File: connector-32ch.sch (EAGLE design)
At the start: 67 parts, among them X1 OMNETICS_36PAD

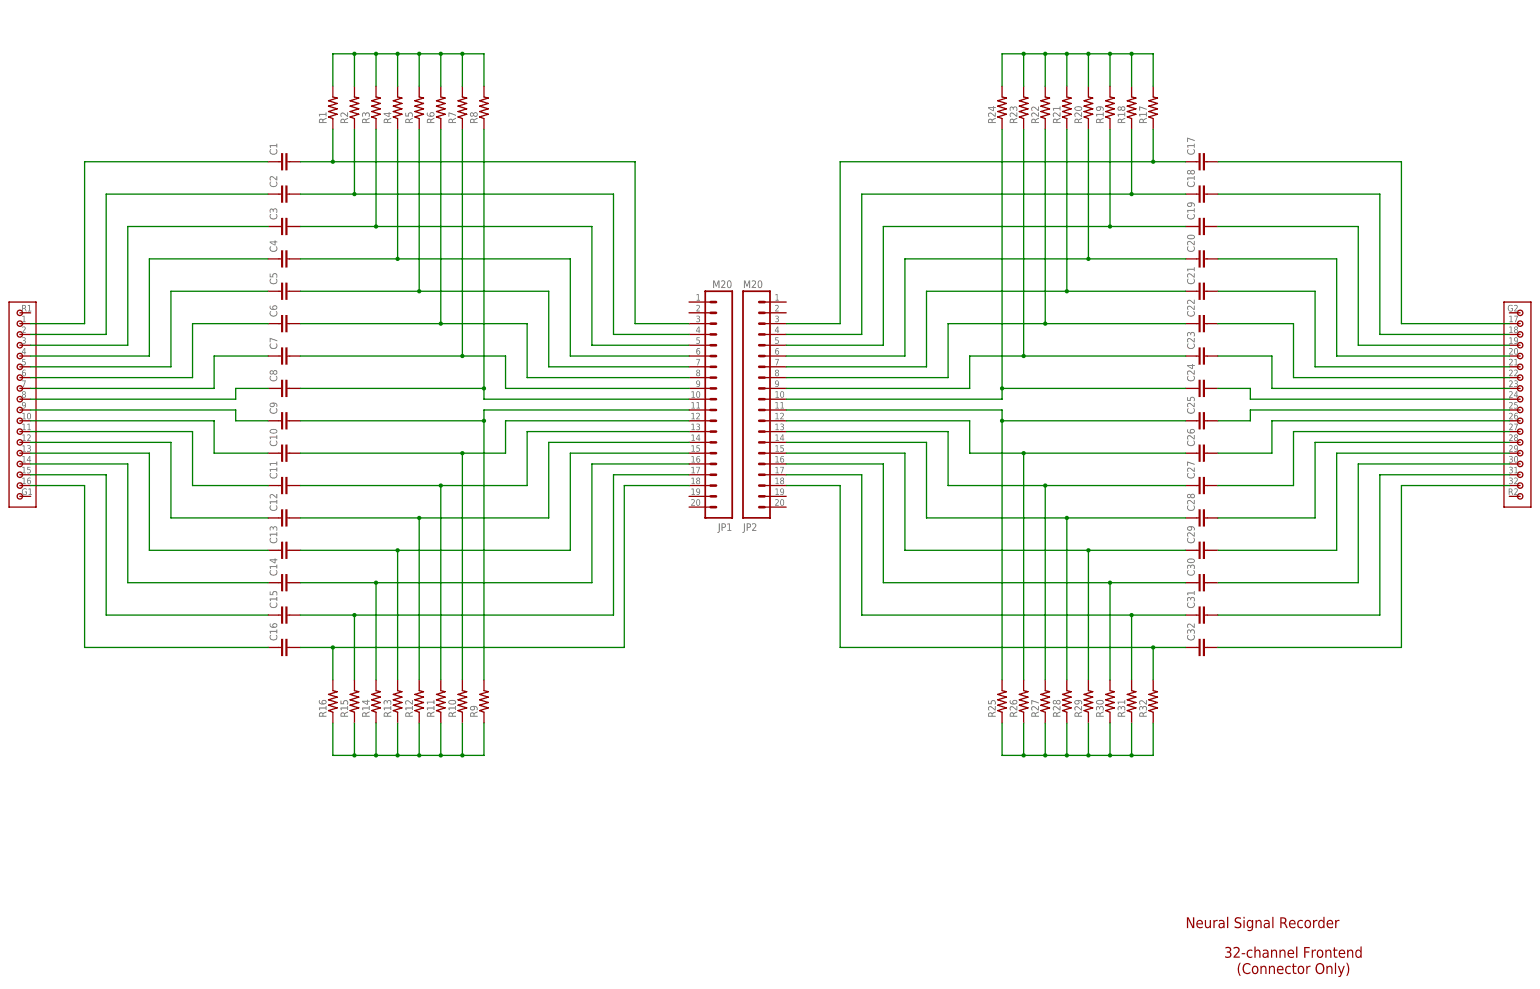
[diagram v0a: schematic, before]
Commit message: finished neural connector board.
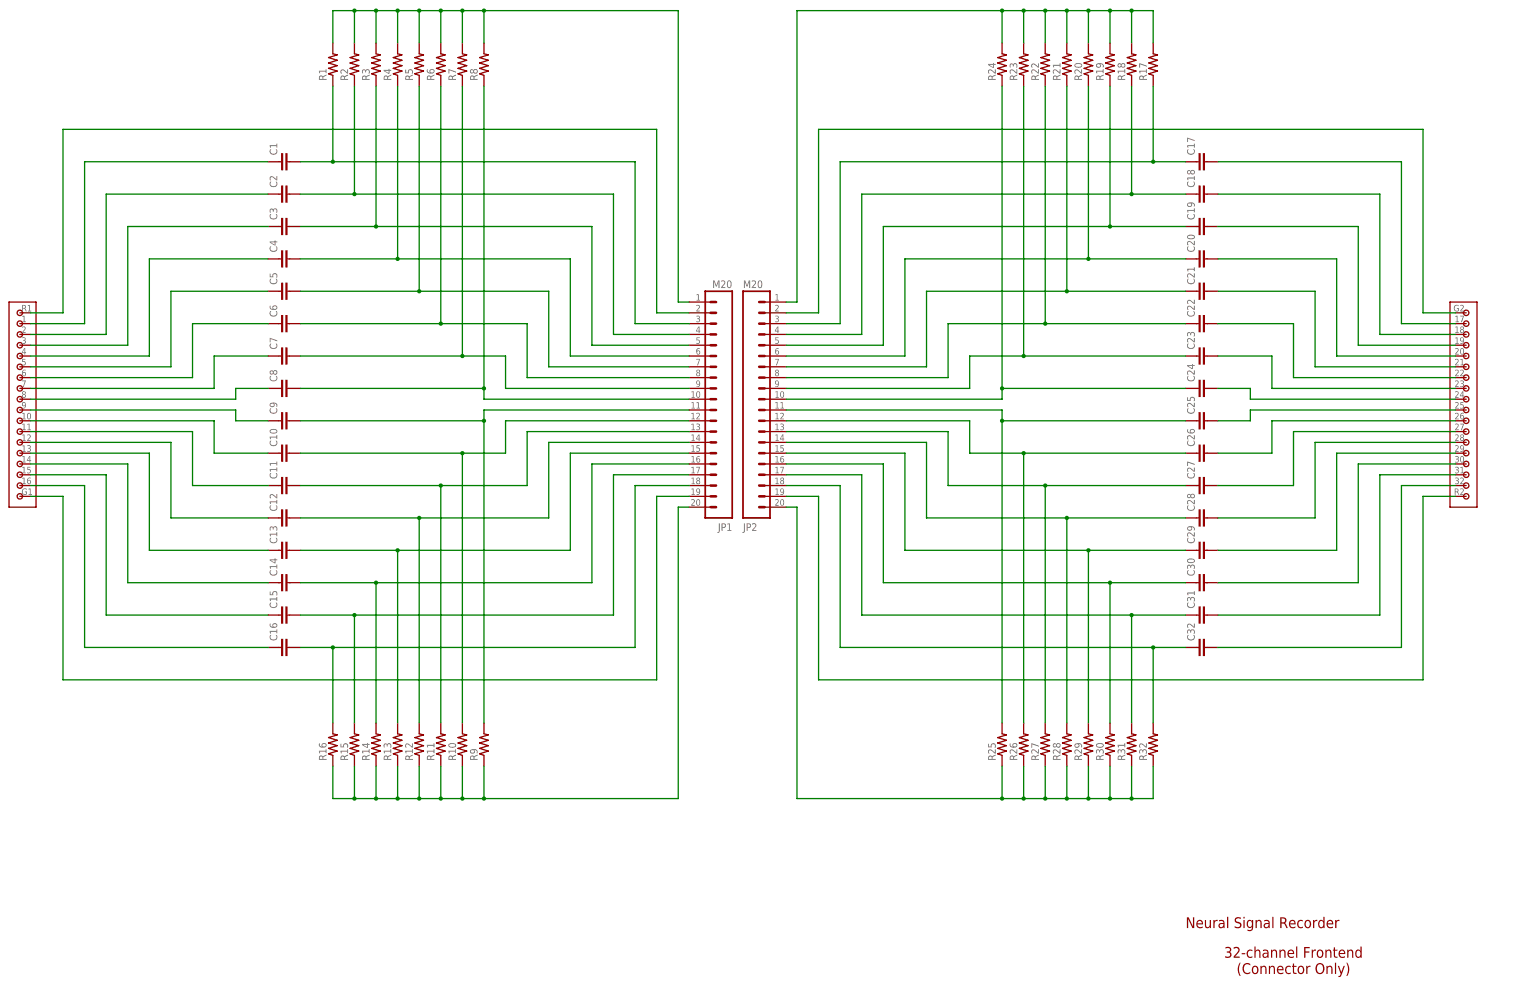
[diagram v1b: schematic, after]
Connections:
- removed net N$65: R1.2, R2.2, R3.2, R4.2, R5.2, R6.2, R7.2, R8.2
- removed net N$66: R17.2, R18.2, R19.2, R20.2, R21.2, R22.2, R23.2, R24.2
- removed net N$67: R10.1, R11.1, R12.1, R13.1, R14.1, R15.1, R16.1, R9.1
- removed net N$68: R25.1, R26.1, R27.1, R28.1, R29.1, R30.1, R31.1, R32.1
- new net G: JP1.19, JP2.19, X1A.P$18, X1B.P$18
- new net R: JP1.2, JP2.2, X1A.P$1, X1B.P$1
- new net VCM: JP1.1, JP1.20, JP2.1, JP2.20, R1.2, R10.1, R11.1, R12.1, R13.1, R14.1, R15.1, R16.1, R17.2, R18.2, R19.2, R2.2, R20.2, R21.2, R22.2, R23.2, R24.2, R25.1, R26.1, R27.1, R28.1, R29.1, R3.2, R30.1, R31.1, R32.1, R4.2, R5.2, R6.2, R7.2, R8.2, R9.1
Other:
- moved on the sheet: R1, R10, R11, R12, R13, R14, R15, R16, R17, R18, R19, R2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

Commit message: almost final board files
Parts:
- C1, C10, C11, C12, C13, C14, C15, C16, C17, C18, C19, C2, C20, C21, C22, C23, C24, C25, C26, C27, C28, C29, C3, C30, C31, C32, C4, C5, C6, C7, C8, C9: value (none) -> 22nf
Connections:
- net G: now also JP1.2, X1A.P$1; no longer JP1.19, X1A.P$18
- net R: now also JP1.19, X1A.P$18; no longer JP1.2, X1A.P$1
